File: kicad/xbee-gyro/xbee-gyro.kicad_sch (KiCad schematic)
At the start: 18 parts, among them J1 IMU_in, J2 IMU, J3 XBee, SW1 Reset, U1 XBEE-S2C

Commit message: no message
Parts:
- removed J1: IMU_in, Connector_PinHeader_1.27mm:PinHeader_1x05_P1.27mm_Vertical, symbol Connector_Generic:Conn_01x05
- removed J2: IMU, Connector_PinSocket_2.54mm:PinSocket_1x05_P2.54mm_Vertical, symbol Connector_Generic:Conn_01x05
- removed J3: XBee, Connector_PinSocket_2.54mm:PinSocket_1x04_P2.54mm_Vertical, symbol Connector_Generic:Conn_01x04
- added C1, C3: 10u, Capacitor_SMD:C_0603_1608Metric_Pad1.08x0.95mm_HandSolder, symbol Device:C
- added C2: 0.1u, Capacitor_SMD:C_0603_1608Metric_Pad1.08x0.95mm_HandSolder, symbol Device:C
- added D1: LED(OSWT1608), 0.main.robot:LED_SMLE13WBC8W1, symbol Device:LED
- added D2, D3: RSX101VAM-30, Diode_SMD:D_0805_2012Metric_Pad1.15x1.40mm_HandSolder, symbol Device:D
- added J1: Trimmer, 0.main.robot:JSTS6B-ZRLFSN, symbol Connector_Generic:Conn_01x06
- added J2: Conn_01x12, Connector_PinHeader_2.54mm:PinHeader_2x06_P2.54mm_Vertical, symbol Connector_Generic:Conn_01x12
- added R1, R2, R3: 47k, Resistor_SMD:R_0603_1608Metric_Pad0.98x0.95mm_HandSolder, symbol Device:R
- added R4: 470, Resistor_SMD:R_0603_1608Metric_Pad0.98x0.95mm_HandSolder, symbol Device:R
- added R5: 10k, Resistor_SMD:R_0603_1608Metric_Pad0.98x0.95mm_HandSolder, symbol Device:R
- added RV1, RV2, RV3, RV4, RV5: 20K, 0.main.robot:Trim-GF063P, symbol control20220206-rescue:R_POT-Device
- added SW1: RESET, 0.main.robot:TVAF06-A020B-R, symbol Switch:SW_Push
- added U1: ATmega328P-AU, Package_QFP:TQFP-32_7x7mm_P0.8mm, symbol MCU_Microchip_ATmega:ATmega328P-A
- added Y1: 8Mhz, Crystal:Resonator-3Pin_W6.0mm_H3.0mm, symbol Device:Crystal_GND2
- gave numbers to parts that had none: 3
- renumbered D1 to D4, D2 to D5, D3 to D6, R5 to R10, R6 to R11, R7 to R12, R1 to R6, R2 to R7, R3 to R8, R4 to R9, SW1 to SW2, U1 to U2
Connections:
- net +5V: now also J2.2 (Pin_2)
- net GND: now also C1.2, C2.2, C3.2, D1.1 (K), J2.4 (Pin_4), SW1.1, U1.21 (GND), U1.3 (GND), U1.5 (GND), Y1.2
- net XBee_2: now reaches R11.2
- net XBee_2: now also J2.6 (Pin_6)
- net XBee_1: now reaches R10.2, R12.1
- net XBee_1: now also J2.5 (Pin_5)
- new net: J1.1 (Pin_1), RV1.2, RV1.3, U1.23 (PC0)
- new net: J1.2 (Pin_2), RV2.2, RV2.3, U1.24 (PC1)
- new net: J1.3 (Pin_3), RV3.2, RV3.3, U1.25 (PC2)
- new net: J1.4 (Pin_4), RV4.2, RV4.3, U1.26 (PC3)
- new net: D3.2 (A), J1.6 (Pin_6), RV1.1, RV2.1, RV3.1, RV4.1, RV5.1
- new net: R1.1, U1.22 (ADC7)
- new net: R4.1, U1.10 (PD6)
- new net: D1.2 (A), R4.2
- new net: U1.7 (XTAL1/PB6), Y1.3
- new net: U1.8 (XTAL2/PB7), Y1.1
- new net +3V3: C1.1, C2.1, D2.1 (K), D3.1 (K), J2.1 (Pin_1), R1.2, R2.1, R3.1, R5.2, U1.18 (AVCC), U1.4 (VCC), U1.6 (VCC)
- new net ICSP_1: J2.9 (Pin_9), U1.16 (PB4)
- new net ICSP_3: J2.10 (Pin_10), U1.17 (PB5)
- new net ICSP_4: J2.11 (Pin_11), U1.15 (PB3)
- new net ICSP_5: C3.1, D2.2 (A), J2.12 (Pin_12), R5.1, SW1.2, U1.29 (~{RESET}/PC6)
- new net Line5: J1.5 (Pin_5), RV5.2, RV5.3, U1.19 (ADC6)
- new net OLED_SCL: J2.7 (Pin_7), R2.2, U1.28 (PC5)
- new net OLED_SDA: J2.8 (Pin_8), R3.2, U1.27 (PC4)
- no-connect marks 14 -> 25
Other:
- note added: "(Trimmer section)"
- note added: "A0"
- note added: "A1"
- note added: "A2"
- note added: "A3"
- note added: "A5"
- note added: "Line 1"
- note added: "Line 2"
- note added: "Line 3"
- note added: "Line 4"
- note added: "Line 5"

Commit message: add: xbee-gyro
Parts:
- removed C1, C3, C4, C5: 10u, Capacitor_SMD:C_0603_1608Metric_Pad1.08x0.95mm_HandSolder, symbol Device:C
- removed C2: 0.1u, Capacitor_SMD:C_0603_1608Metric_Pad1.08x0.95mm_HandSolder, symbol Device:C
- removed D1: LED(OSWT1608), 0.main.robot:LED_SMLE13WBC8W1, symbol Device:LED
- removed D2, D3: RSX101VAM-30, Diode_SMD:D_0805_2012Metric_Pad1.15x1.40mm_HandSolder, symbol Device:D
- removed J1: Trimmer, 0.main.robot:JSTS6B-ZRLFSN, symbol Connector_Generic:Conn_01x06
- removed J2: Conn_01x12, Connector_PinHeader_2.54mm:PinHeader_2x06_P2.54mm_Vertical, symbol Connector_Generic:Conn_01x12
- removed R1, R2, R3: 47k, Resistor_SMD:R_0603_1608Metric_Pad0.98x0.95mm_HandSolder, symbol Device:R
- removed R4: 470, Resistor_SMD:R_0603_1608Metric_Pad0.98x0.95mm_HandSolder, symbol Device:R
- removed R5: 10k, Resistor_SMD:R_0603_1608Metric_Pad0.98x0.95mm_HandSolder, symbol Device:R
- removed RV1, RV2, RV3, RV4, RV5: 20K, 0.main.robot:Trim-GF063P, symbol control20220206-rescue:R_POT-Device
- removed SW1: RESET, 0.main.robot:TVAF06-A020B-R, symbol Switch:SW_Push
- removed U1: ATmega328P-AU, Package_QFP:TQFP-32_7x7mm_P0.8mm, symbol MCU_Microchip_ATmega:ATmega328P-A
- removed U3: AZ1117CH-3.3, Package_TO_SOT_SMD:SOT-223-3_TabPin2, symbol Regulator_Linear:AZ1084-2.85
- removed Y1: 8Mhz, Crystal:Resonator-3Pin_W6.0mm_H3.0mm, symbol Device:Crystal_GND2
- added C1: 0.1u, Capacitor_SMD:C_0603_1608Metric_Pad1.08x0.95mm_HandSolder, symbol 0.main.mega:C
- added J1: IMU_in, Connector_PinHeader_1.27mm:PinHeader_1x05_P1.27mm_Vertical, symbol Connector_Generic:Conn_01x05
- added J2: IMU, Connector_PinSocket_2.54mm:PinSocket_1x05_P2.54mm_Vertical, symbol Connector_Generic:Conn_01x05
- added J3: XBee, Connector_PinSocket_2.54mm:PinSocket_1x04_P2.54mm_Vertical, symbol Connector_Generic:Conn_01x04
- added U2: XC6216D_SOT89, Package_TO_SOT_SMD:SOT-89-3, symbol Regulator_Linear:XC6216D_SOT89
- renumbered D4 to D1, D5 to D2, D6 to D3, R6 to R1, R7 to R2, R8 to R3, R9 to R4, R10 to R5, R11 to R6, R12 to R7, SW2 to SW1, U2 to U1
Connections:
- net +5V: now also C1.1, J3.2 (Pin_2), U2.3 (IN)
- net GND: now also C1.2, J3.4 (Pin_4), U2.2 (GND)
- net at R2.1, R3.1, U1.1 (VDD): now also U2.1 (OUT)
- net XBee_1: no longer names the net of R5.2, R7.1
- net XBee_1: now also J3.1 (Pin_1)
- net XBee_2: no longer names the net of R6.2
- net XBee_2: now also J3.3 (Pin_3)
- new net: J1.1 (Pin_1), J2.1 (Pin_1)
- new net: J1.2 (Pin_2), J2.2 (Pin_2)
- new net: J1.3 (Pin_3), J2.3 (Pin_3)
- new net: J1.4 (Pin_4), J2.4 (Pin_4)
- new net: J1.5 (Pin_5), J2.5 (Pin_5)
- no-connect marks 25 -> 14
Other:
- note removed: "(Trimmer section)"
- note removed: "A0"
- note removed: "A1"
- note removed: "A2"
- note removed: "A3"
- note removed: "A5"
- note removed: "Line 1"
- note removed: "Line 2"
- note removed: "Line 3"
- note removed: "Line 4"
- note removed: "Line 5"

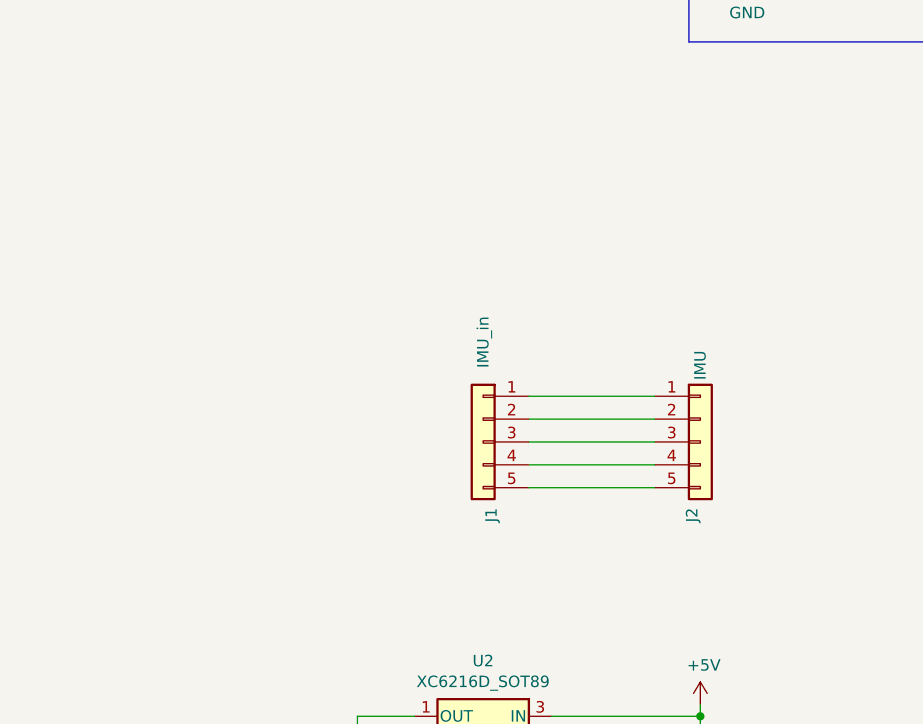
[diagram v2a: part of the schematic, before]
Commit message: IMU and Xbee board change
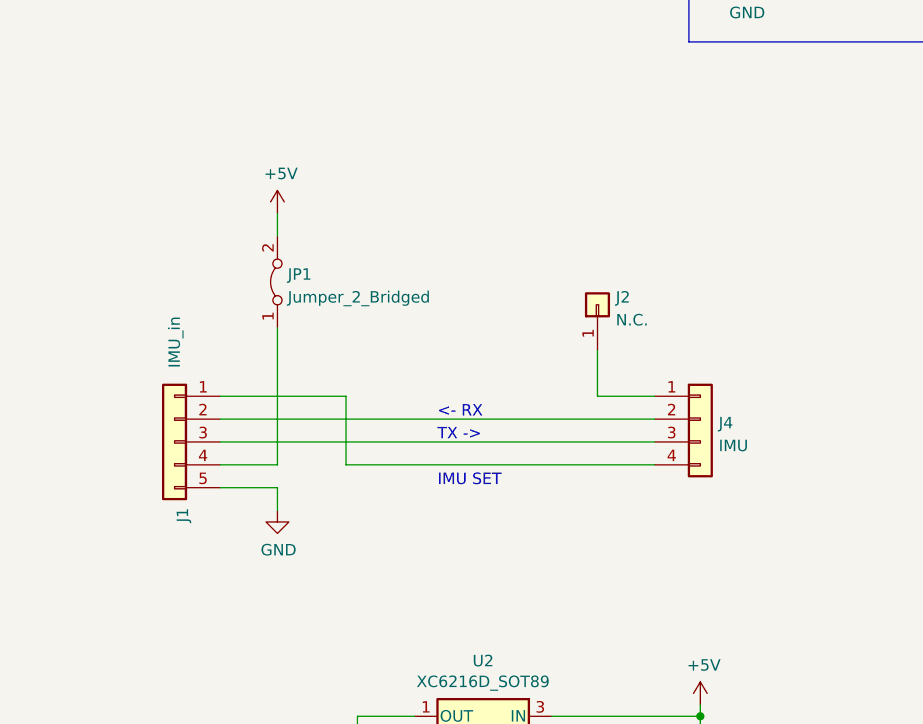
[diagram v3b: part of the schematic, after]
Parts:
- removed J2: IMU, Connector_PinSocket_2.54mm:PinSocket_1x05_P2.54mm_Vertical, symbol Connector_Generic:Conn_01x05
- added J2: N.C., Connector_PinHeader_2.54mm:PinHeader_1x01_P2.54mm_Vertical, symbol Connector_Generic:Conn_01x01
- added J4: IMU, Connector_PinSocket_2.54mm:PinSocket_1x04_P2.54mm_Vertical, symbol Connector_Generic:Conn_01x04
- added JP1: Jumper_2_Bridged, Jumper:SolderJumper-2_P1.3mm_Bridged_Pad1.0x1.5mm, symbol Jumper:Jumper_2_Bridged
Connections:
- net +5V: now also JP1.2 (B)
- net GND: now also J1.5 (Pin_5)
- net at J1.1 (Pin_1): now also J4.4 (Pin_4)
- net at J1.2 (Pin_2): now also J4.2 (Pin_2)
- net at J1.3 (Pin_3): now also J4.3 (Pin_3)
- net at J1.4 (Pin_4): now also JP1.1 (A)
- new net: J2.1 (Pin_1), J4.1 (Pin_1)
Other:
- note added: "<- RX"
- note added: "IMU SET"
- note added: "TX ->"
- title: control board -> IMU&Xbee board
- moved on the sheet: J1
